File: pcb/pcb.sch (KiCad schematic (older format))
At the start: 6 parts

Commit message: pcb pinout + protections
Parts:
- added D?: Vz=3v3, symbol Device:D_Zener_Small
- added D?: Vz=15, symbol Device:D_Zener_Small
- added D?: 4148, symbol Device:D_Small
- added FH?: F5196-ND, project:Blade Fuse Holder, symbol Device:Fuse_Small
- added J?: Screw_Terminal_01x04, symbol Connector:Screw_Terminal_01x04
- added J?: Screw_Terminal_01x03, symbol Connector:Screw_Terminal_01x03
- added J?: Screw_Terminal_01x02, symbol Connector:Screw_Terminal_01x02
- added SW?: SW_SPDT, symbol Switch:SW_SPDT
- J?: value Conn_01x04_Male -> keyed molex
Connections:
- net labels added: D1, D2, D5, D6, D7, D8, GPIO0, RXD, TXD, UNLOCK_PIN, VBUS
- wire segments 46 -> 76
- no-connect marks 0 -> 2
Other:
- note added: "D4 is on-board LED for NodeMCU V3"
- note added: "TODO: zener diode/rpp on 3v3\nTODO: UART connector\nTODO: figure out EN pin\nTODO: link data sheet\nTODO: GPIO0 programming switch"
- note added: "lolin already has on-board reset button"
- note added: "relay connector"
- moved on the sheet: J?

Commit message: added esp board datasheet to sch symbol
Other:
- note added: "TODO: zener diode/rpp on 3v3\nTODO: UART connector\nTODO: figure out EN pin\nTODO: link data sheet\nTODO: GPIO0 programming switch\nTODO: LED for prog mode"
- note removed: "TODO: zener diode/rpp on 3v3\nTODO: UART connector\nTODO: figure out EN pin\nTODO: link data sheet\nTODO: GPIO0 programming switch"
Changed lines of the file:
@@
 F 1 "lolinv3" H 6200 3484 50  0000 C CNN
 F 2 "project:lolinv3" H 6250 3450 50  0001 C CNN
-F 3 "" H 6250 3450 50  0001 C CNN
+F 3 "${KIPRJMOD}/../docs/NodeMCU-V3.pdf" H 6250 3450 50  0001 C CNN
 	1    5850 3350
 	1    0    0    -1
@@
 	2500 6100 2550 6100
 Text Notes 4550 1950 0    50   ~ 0
-TODO: zener diode/rpp on 3v3\nTODO: UART connector\nTODO: figure out EN pin\nTODO: link data sheet\nTODO: GPIO0 programming switch
+TODO: zener diode/rpp on 3v3\nTODO: UART connector\nTODO: figure out EN pin\nTODO: link data sheet\nTODO: GPIO0 programming switch\nTODO: LED for prog mode
 $Comp
 L Connector:Screw_Terminal_01x02 J?

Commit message: updated esp board symbol name to its common name
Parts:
- removed U?: lolinv3, project:lolinv3, symbol project:lolinv3
- added U?: NodeMCUv3, project:lolinv3, symbol project:NodeMCUv3
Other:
- note added: "D3 is GPIO0 (used for programming)\nD4 is on-board LED for NodeMCU V3\nRST already has reset button on-board"
- note removed: "D4 is on-board LED for NodeMCU V3"
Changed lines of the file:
@@
 $EndDescr
 $Comp
-L project:lolinv3 U?
-U 1 1 625B736B
-P 5850 3350
-F 0 "U?" H 6200 3575 50  0000 C CNN
-F 1 "lolinv3" H 6200 3484 50  0000 C CNN
-F 2 "project:lolinv3" H 6250 3450 50  0001 C CNN
-F 3 "${KIPRJMOD}/../docs/NodeMCU-V3.pdf" H 6250 3450 50  0001 C CNN
-	1    5850 3350
-	1    0    0    -1
-$EndComp
-$Comp
 L Connector:Conn_01x04_Male J?
 U 1 1 625B8421
@@
 U 1 1 625D8F0E
 P 7150 4350
-F 0 "J?" H 7068 3725 50  0000 C CNN
-F 1 "Screw_Terminal_01x09" H 7600 3800 50  0000 C CNN
+F 0 "J?" H 7650 4200 50  0000 C CNN
+F 1 "Screw_Terminal_01x09" H 7750 4350 50  0000 C CNN
 F 2 "" H 7150 4350 50  0001 C CNN
 F 3 "~" H 7150 4350 50  0001 C CNN
@@
 Text Label 5800 4650 2    50   ~ 0
 D1
-Text Notes 5350 5150 0    50   ~ 0
-D4 is on-board LED for NodeMCU V3
+Text Notes 5300 5350 0    50   ~ 0
+D3 is GPIO0 (used for programming)\nD4 is on-board LED for NodeMCU V3\nRST already has reset button on-board
 $Bitmap
 Pos 2000 1700
@@
 Wire Wire Line
 	5800 4450 5850 4450
+$Comp
+L project:NodeMCUv3 U?
+U 1 1 6299BF2F
+P 5850 3350
+F 0 "U?" H 6200 3575 50  0000 C CNN
+F 1 "NodeMCUv3" H 6200 3484 50  0000 C CNN
+F 2 "project:lolinv3" H 6250 3450 50  0001 C CNN
+F 3 "${KIPRJMOD}/../docs/NodeMCU-V3.pdf" H 6250 3450 50  0001 C CNN
+	1    5850 3350
+	1    0    0    -1
+$EndComp
 $EndSCHEMATC

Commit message: major schematic reorg+documentation
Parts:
- removed D?: 4148, symbol Device:D_Small
- removed J? (x2): Screw_Terminal_01x09, symbol Connector:Screw_Terminal_01x09
- removed J? (x2): Screw_Terminal_01x04, symbol Connector:Screw_Terminal_01x04
- removed SW?: SW_SPDT, symbol Switch:SW_SPDT
- added D? (x2): 1N4148, Diode_THT:D_DO-35_SOD27_P7.62mm_Horizontal, symbol Device:D_Small
- added D? (x2): GN, symbol Device:LED_Small
- added D?: RD, symbol Device:LED_Small
- added J?: pin header, symbol Connector:Conn_01x01_Male
- added J?: Screw_Terminal_01x06, symbol Connector:Screw_Terminal_01x06
- added J?: Screw_Terminal_01x07, symbol Connector:Screw_Terminal_01x07
- added J? (x2): Screw_Terminal_01x04, symbol Connector:Screw_Terminal_01x04
- added R? (x3): 1k, symbol Device:R_Small
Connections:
- net labels added: GPIO_0
- net labels removed: D1, D2, D5, D6, D7, D8, GPIO0
- wire segments 76 -> 87
- no-connect marks 2 -> 3
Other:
- note added: "- 3V3 needs reverse polarity\n- VBUS already has protections"
- note added: "- over current protection using fuse\n- over voltage protection using zener diode\n- reverse polarity protection using 1n4148\n- use blade fuses + fuse holder for easy replacement\n- fuse before zener diode\n - zener diode shorts (kinda) on V>15\n - fuse (hopefully) blows on current surge\n- 15V is max allowed Vin\n - NodeMCU V3 likely uses AMS1117 lin reg\n - max Vin of 15V\n - very common regul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"
- note added: "ESP Breakout"
- note added: "Goal: Provide cleaner package for door controller than\ncurrently existing breadboard solution\n\nAHA Requirements\n-------------------------\n- Seat NodeMCU V3 dev board\n- Connect to relay (UNLOCK_PIN)\n- Expose UART for NFC reader (Serial/Serial0)\n- Accept 12V/USB from in-place power supply\n- Expose unused GPIO pins\n- Simple\n- Through-hole components\n\nEngineering Requirements\n----------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"
- note added: "Indicators + I/O"
- note added: "Overview"
- note added: "Pins to Not Expose\n-------------------------\n- D3 is GPIO0 (used for programming)\n- D4 is on-board LED for NodeMCU (already used)\n- RST connected to on-NodeMCU reset button (no need)\n- EN likely unused; connect to pin header just in case (special pin)\n- 10 (3V3) boxed in by D1,D2,D3 traces (no point)"
- note added: "Power Connectors"
- note added: "Power Input (5-15V)"
- note added: "Power Outputs"
- note added: "\n\n\n\nFIRST USAGE\n-------------------------\n1. Connect NFC comms wires to 4-pin molex connector\n2. Connect relay pwr, gnd, sig to relay screw terminal\n3. Check that a fuse is in the fuse holder (FH1)\n4. Connect 12VDC power brick to "Power In" connector\n5. Verify "VBUS" LED is lit. Relay may also click/LEDs\n6. Remove blade fuse (LEDs should go dim)\n7. Program NodeMCU V3 with firmware in 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"
- note removed: "D3 is GPIO0 (used for programming)\nD4 is on-board LED for NodeMCU V3\nRST already has reset button on-board"
- note removed: "TODO: zener diode/rpp on 3v3\nTODO: UART connector\nTODO: figure out EN pin\nTODO: link data sheet\nTODO: GPIO0 programming switch\nTODO: LED for prog mode"
- note removed: "lolin already has on-board reset button"
- note removed: "relay connector"
- moved on the sheet: D?, FH?, J?, U?

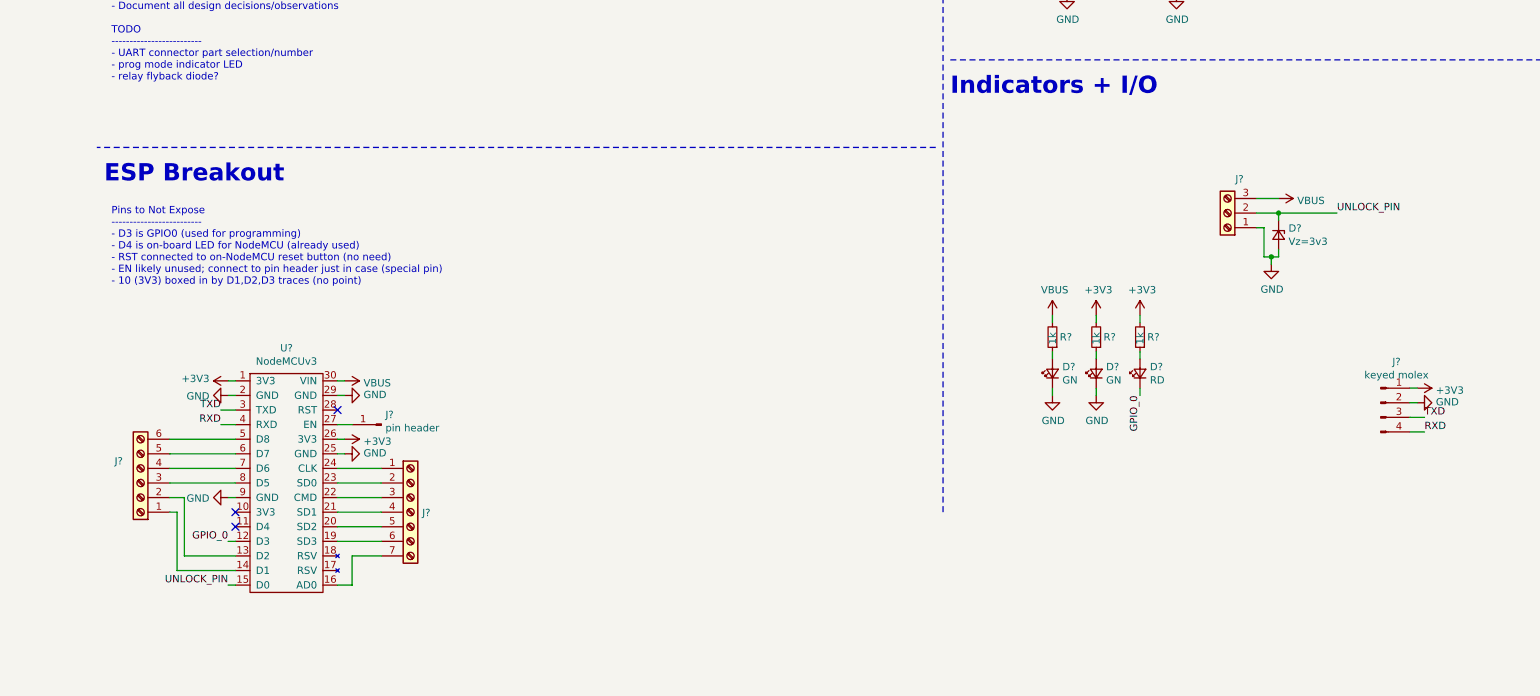
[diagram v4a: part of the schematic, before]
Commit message: UNLOCK_PIN change and connector selection for relay
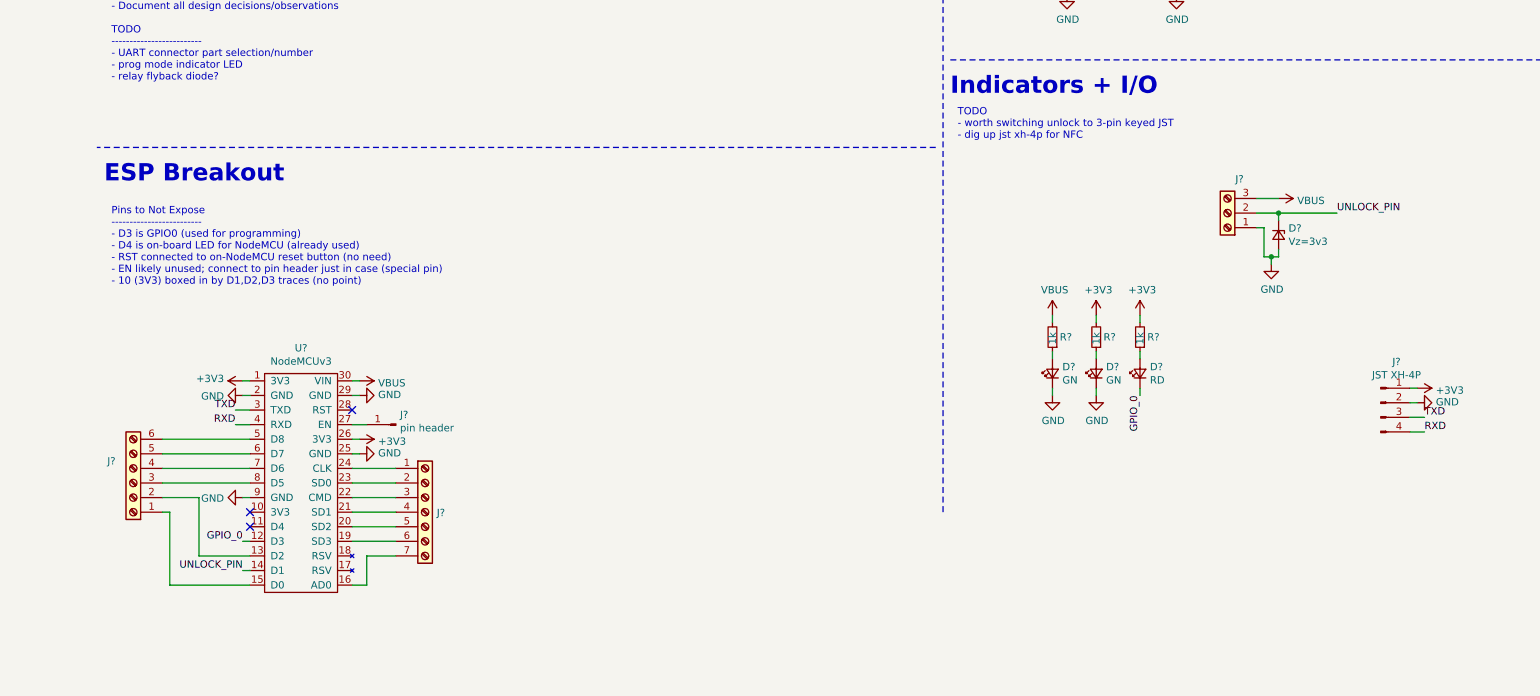
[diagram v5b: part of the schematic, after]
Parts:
- J?: value keyed molex -> JST XH-4P
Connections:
- net UNLOCK_PIN: now also U?.14 (D1); no longer U?.15 (D0)
- net at J?.1 (Pin_1): now also U?.15 (D0); no longer U?.14 (D1)
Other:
- note added: "TODO\n- worth switching unlock to 3-pin keyed JST\n- dig up jst xh-4p for NFC"
- moved on the sheet: J?, U?
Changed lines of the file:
@@
 P 9300 6000
 F 0 "J?" H 9408 6281 50  0000 C CNN
-F 1 "keyed molex" H 9408 6190 50  0000 C CNN
+F 1 "JST XH-4P" H 9408 6190 50  0000 C CNN
 F 2 "" H 9300 6000 50  0001 C CNN
-F 3 "~" H 9300 6000 50  0001 C CNN
+F 3 "https://www.amazon.com/GeeBat-460pcs-Connector-Housing-Adapter/dp/B01MCZE2HM/" H 9300 6000 50  0001 C CNN
 	1    9300 6000
 	1    0    0    -1
@@
 $EndBitmap
 Wire Wire Line
-	2150 7250 2250 7250
+	2250 7250 2350 7250
 Wire Wire Line
-	1400 7250 1450 7250
-Text Label 1400 7250 2    50   ~ 0
+	1500 7150 1550 7150
+Text Label 1500 7150 2    50   ~ 0
 UNLOCK_PIN
 $Comp
 L power:VBUS #PWR?
 U 1 1 627D4DE7
-P 2200 5850
-F 0 "#PWR?" H 2200 5700 50  0001 C CNN
-F 1 "VBUS" V 2215 5978 50  0000 L CNN
-F 2 "" H 2200 5850 50  0001 C CNN
-F 3 "" H 2200 5850 50  0001 C CNN
-	1    2200 5850
+P 2300 5850
+F 0 "#PWR?" H 2300 5700 50  0001 C CNN
+F 1 "VBUS" V 2315 5978 50  0000 L CNN
+F 2 "" H 2300 5850 50  0001 C CNN
+F 3 "" H 2300 5850 50  0001 C CNN
+	1    2300 5850
 	0    1    1    0
 $EndComp
 Wire Wire Line
-	2200 5850 2150 5850
+	2300 5850 2250 5850
 $Comp
 L power:GND #PWR?
 U 1 1 6289091D
-P 2200 5950
-F 0 "#PWR?" H 2200 5700 50  0001 C CNN
-F 1 "GND" V 2205 5822 50  0000 R CNN
-F 2 "" H 2200 5950 50  0001 C CNN
-F 3 "" H 2200 5950 50  0001 C CNN
-	1    2200 5950
+P 2300 5950
+F 0 "#PWR?" H 2300 5700 50  0001 C CNN
+F 1 "GND" V 2305 5822 50  0000 R CNN
+F 2 "" H 2300 5950 50  0001 C CNN
+F 3 "" H 2300 5950 50  0001 C CNN
+	1    2300 5950
 	0    -1   -1   0
 $EndComp
 Wire Wire Line
-	2200 5950 2150 5950
+	2300 5950 2250 5950
 $Comp
 L power:+3V3 #PWR?
 U 1 1 6289B298
-P 1400 5850
-F 0 "#PWR?" H 1400 5700 50  0001 C CNN
-F 1 "+3V3" V 1415 5978 50  0000 L CNN
-F 2 "" H 1400 5850 50  0001 C CNN
-F 3 "" H 1400 5850 50  0001 C CNN
-	1    1400 5850
+P 1500 5850
+F 0 "#PWR?" H 1500 5700 50  0001 C CNN
+F 1 "+3V3" V 1515 5978 50  0000 L CNN
+F 2 "" H 1500 5850 50  0001 C CNN
+F 3 "" H 1500 5850 50  0001 C CNN
+	1    1500 5850
 	0    -1   -1   0
 $EndComp
 Wire Wire Line
-	1400 5850 1450 5850
+	1500 5850 1550 5850
 $Comp
 L power:GND #PWR?
 U 1 1 6289D808
-P 1400 5950
-F 0 "#PWR?" H 1400 5700 50  0001 C CNN
-F 1 "GND" V 1405 5822 50  0000 R CNN
-F 2 "" H 1400 5950 50  0001 C CNN
-F 3 "" H 1400 5950 50  0001 C CNN
-	1    1400 5950
+P 1500 5950
+F 0 "#PWR?" H 1500 5700 50  0001 C CNN
+F 1 "GND" V 1505 5822 50  0000 R CNN
+F 2 "" H 1500 5950 50  0001 C CNN
+F 3 "" H 1500 5950 50  0001 C CNN
+	1    1500 5950
 	0    1    1    0
 $EndComp
 Wire Wire Line
-	1400 5950 1450 5950
+	1500 5950 1550 5950
 $Comp
 L power:GND #PWR?
 U 1 1 628A269C
-P 1400 6650
-F 0 "#PWR?" H 1400 6400 50  0001 C CNN
-F 1 "GND" V 1405 6522 50  0000 R CNN
-F 2 "" H 1400 6650 50  0001 C CNN
-F 3 "" H 1400 6650 50  0001 C CNN
-	1    1400 6650
+P 1500 6650
+F 0 "#PWR?" H 1500 6400 50  0001 C CNN
+F 1 "GND" V 1505 6522 50  0000 R CNN
+F 2 "" H 1500 6650 50  0001 C CNN
+F 3 "" H 1500 6650 50  0001 C CNN
+	1    1500 6650
 	0    1    1    0
 $EndComp
 Wire Wire Line
-	1400 6650 1450 6650
+	1500 6650 1550 6650
 $Comp
 L power:GND #PWR?
 U 1 1 628A8319
-P 2200 6350
-F 0 "#PWR?" H 2200 6100 50  0001 C CNN
-F 1 "GND" V 2205 6222 50  0000 R CNN
-F 2 "" H 2200 6350 50  0001 C CNN
-F 3 "" H 2200 6350 50  0001 C CNN
-	1    2200 6350
+P 2300 6350
+F 0 "#PWR?" H 2300 6100 50  0001 C CNN
+F 1 "GND" V 2305 6222 50  0000 R CNN
+F 2 "" H 2300 6350 50  0001 C CNN
+F 3 "" H 2300 6350 50  0001 C CNN
+	1    2300 6350
 	0    -1   -1   0
 $EndComp
 Wire Wire Line
-	2200 6350 2150 6350
+	2300 6350 2250 6350
 $Comp
 L power:+3V3 #PWR?
 U 1 1 628AA533
-P 2200 6250
-F 0 "#PWR?" H 2200 6100 50  0001 C CNN
-F 1 "+3V3" V 2215 6378 50  0000 L CNN
-F 2 "" H 2200 6250 50  0001 C CNN
-F 3 "" H 2200 6250 50  0001 C CNN
-	1    2200 6250
+P 2300 6250
+F 0 "#PWR?" H 2300 6100 50  0001 C CNN
+F 1 "+3V3" V 2315 6378 50  0000 L CNN
+F 2 "" H 2300 6250 50  0001 C CNN
+F 3 "" H 2300 6250 50  0001 C CNN
+	1    2300 6250
 	0    1    1    0
 $EndComp
 Wire Wire Line
-	2200 6250 2150 6250
-NoConn ~ 2150 6050
-Text Label 1350 6050 2    50   ~ 0
+	2300 6250 2250 6250
+NoConn ~ 2250 6050
+Text Label 1450 6050 2    50   ~ 0
 TXD
-Text Label 1350 6150 2    50   ~ 0
+Text Label 1450 6150 2    50   ~ 0
 RXD
 Wire Wire Line
-	1350 6050 1450 6050
+	1450 6050 1550 6050
 Wire Wire Line
-	1350 6150 1450 6150
-NoConn ~ 1450 6850
-Text Label 1400 6950 2    50   ~ 0
+	1450 6150 1550 6150
+NoConn ~ 1550 6850
+Text Label 1500 6950 2    50   ~ 0
 GPIO_0
 Wire Wire Line
-	1400 6950 1450 6950
+	1500 6950 1550 6950
 $Comp
 L Connector:Conn_01x01_Male J?
 U 1 1 629AF30A
-P 2450 6150
-F 0 "J?" H 2422 6082 50  0000 R CNN
-F 1 "pin header" H 2422 6173 50  0000 R CNN
-F 2 "" H 2450 6150 50  0001 C CNN
-F 3 "~" H 2450 6150 50  0001 C CNN
-	1    2450 6150
+P 2550 6150
+F 0 "J?" H 2522 6082 50  0000 R CNN
+F 1 "pin header" H 2522 6173 50  0000 R CNN
+F 2 "" H 2550 6150 50  0001 C CNN
+F 3 "~" H 2550 6150 50  0001 C CNN
+	1    2550 6150
 	-1   0    0    1
 $EndComp
 Wire Wire Line
-	2250 6150 2150 6150
-NoConn ~ 1450 6750
+	2350 6150 2250 6150
+NoConn ~ 1550 6750
 Wire Wire Line
-	2250 7050 2250 7250
+	2350 7050 2350 7250
 Wire Wire Line
-	2150 6450 2450 6450
+	2250 6450 2550 6450
 Wire Wire Line
-	2150 6550 2450 6550
+	2250 6550 2550 6550
 Wire Wire Line
-	2150 6650 2450 6650
+	2250 6650 2550 6650
 Wire Wire Line
-	2150 6750 2450 6750
+	2250 6750 2550 6750
 Wire Wire Line
-	2150 6850 2450 6850
+	2250 6850 2550 6850
 Wire Wire Line
-	2150 6950 2450 6950
+	2250 6950 2550 6950
 Wire Wire Line
-	2250 7050 2450 7050
+	2350 7050 2550 7050
 $Comp
 L project:NodeMCUv3 U?
 U 1 1 6299BF2F
-P 1450 5850
-F 0 "U?" H 1800 6075 50  0000 C CNN
-F 1 "NodeMCUv3" H 1800 5984 50  0000 C CNN
-F 2 "project:lolinv3" H 1850 5950 50  0001 C CNN
-F 3 "${KIPRJMOD}/../docs/NodeMCU-V3.pdf" H 1850 5950 50  0001 C CNN
-	1    1450 5850
+P 1550 5850
+F 0 "U?" H 1900 6075 50  0000 C CNN
+F 1 "NodeMCUv3" H 1900 5984 50  0000 C CNN
+F 2 "project:lolinv3" H 1950 5950 50  0001 C CNN
+F 3 "${KIPRJMOD}/../docs/NodeMCU-V3.pdf" H 1950 5950 50  0001 C CNN
+	1    1550 5850
 	1    0    0    -1
 $EndComp
 Wire Wire Line
-	1000 6650 1100 6650
+	1200 6650 1200 7050
 Wire Wire Line
-	1100 6650 1100 7050
+	1200 7050 1550 7050
 Wire Wire Line
-	1100 7050 1450 7050
-Wire Wire Line
-	1450 7150 1050 7150
-Wire Wire Line
-	1050 7150 1050 6750
-Wire Wire Line
-	1050 6750 1000 6750
-Wire Wire Line
-	1000 6550 1450 6550
-Wire Wire Line
-	1450 6450 1000 6450
-Wire Wire Line
-	1000 6350 1450 6350
-Wire Wire Line
-	1450 6250 1000 6250
+	1000 6750 950  6750
 $Comp
 L Connector:Screw_Terminal_01x06 J?
 U 1 1 62A0C44B
-P 800 6550
-F 0 "J?" H 950 6400 50  0000 C CNN
-F 1 "Screw_Terminal_01x06" H 1100 6500 50  0001 C CNN
-F 2 "" H 800 6550 50  0001 C CNN
-F 3 "~" H 800 6550 50  0001 C CNN
-	1    800  6550
+P 750 6550
+F 0 "J?" H 900 6400 50  0000 C CNN
+F 1 "Screw_Terminal_01x06" H 1050 6500 50  0001 C CNN
+F 2 "" H 750 6550 50  0001 C CNN
+F 3 "~" H 750 6550 50  0001 C CNN
+	1    750  6550
 	-1   0    0    1
 $EndComp
@@
 L Connector:Screw_Terminal_01x07 J?
 U 1 1 62AD8C42
-P 2650 6750
-F 0 "J?" H 2730 6746 50  0000 L CNN
-F 1 "Screw_Terminal_01x07" H 2730 6701 50  0001 L CNN
-F 2 "" H 2650 6750 50  0001 C CNN
-F 3 "~" H 2650 6750 50  0001 C CNN
-	1    2650 6750
+P 2750 6750
+F 0 "J?" H 2830 6746 50  0000 L CNN
+F 1 "Screw_Terminal_01x07" H 2830 6701 50  0001 L CNN
+F 2 "" H 2750 6750 50  0001 C CNN
+F 3 "~" H 2750 6750 50  0001 C CNN
+	1    2750 6750
 	1    0    0    -1
 $EndComp
@@
 Text Notes 3250 2700 0    50   ~ 0
 \n\n\n\nFIRST USAGE\n-------------------------\n1.  Connect NFC comms wires to 4-pin molex connector\n2.  Connect relay pwr, gnd, sig to relay screw terminal\n3.  Check that a fuse is in the fuse holder (FH1)\n4.  Connect 12VDC power brick to "Power In" connector\n5.  Verify "VBUS" LED is lit. Relay may also click/LEDs\n6.  Remove blade fuse (LEDs should go dim)\n7.  Program NodeMCU V3 with firmware in this repo\n8.  Seat NodeMCU V3 onto board (!!CHECK ORIENTATION!!)\n9.  Re-place blade fuse (VBUS, 3V3 LEDs should light up)\n10. LEDs should light up and door-controller should be functional
+Text Notes 6400 4200 0    50   ~ 0
+TODO\n- worth switching unlock to 3-pin keyed JST\n- dig up jst xh-4p for NFC
+Wire Wire Line
+	1000 7250 1550 7250
+Wire Wire Line
+	1000 6750 1000 7250
+Wire Wire Line
+	950  6650 1200 6650
+Wire Wire Line
+	950  6550 1550 6550
+Wire Wire Line
+	950  6450 1550 6450
+Wire Wire Line
+	950  6350 1550 6350
+Wire Wire Line
+	950  6250 1550 6250
 $EndSCHEMATC
